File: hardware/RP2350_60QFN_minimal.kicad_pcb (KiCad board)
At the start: 4 copper layers, 106.9 x 43.5 mm, 138 parts, among them J1 UJ20-C-H-G-SMT-2A-P16-TR, J2 73101-0570, J3 73101-0570, J4 PinHeader_1x03, J5 4677, SW1 SW_Push, SW2 SW_Push, U1 RP2350_60QFN, U10 ADG621BRMZ, U13 TLP3441TP_F, U15 ADG621BRMZ, U2 REF35330QDBVR, U3 W25Q128JVS, U4 LM27762, U5 NCP1117-3.3_SOT223, U6 MCP47FEB02A0T-E/ST, U7 Opamp_Dual, U8 TLP3441TP_F, Y1 ABM8-272-T3

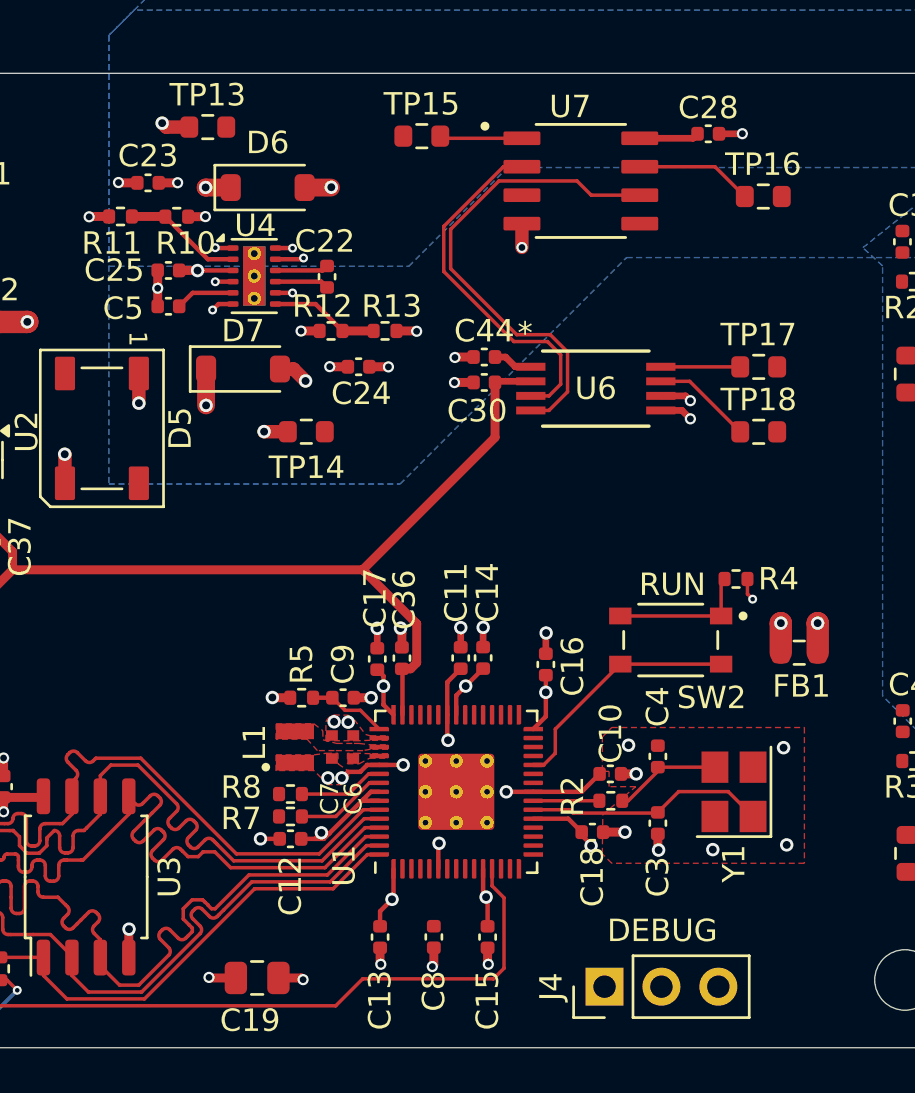
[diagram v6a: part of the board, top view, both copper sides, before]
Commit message: feat(hardware): Connect bottom layer data lines
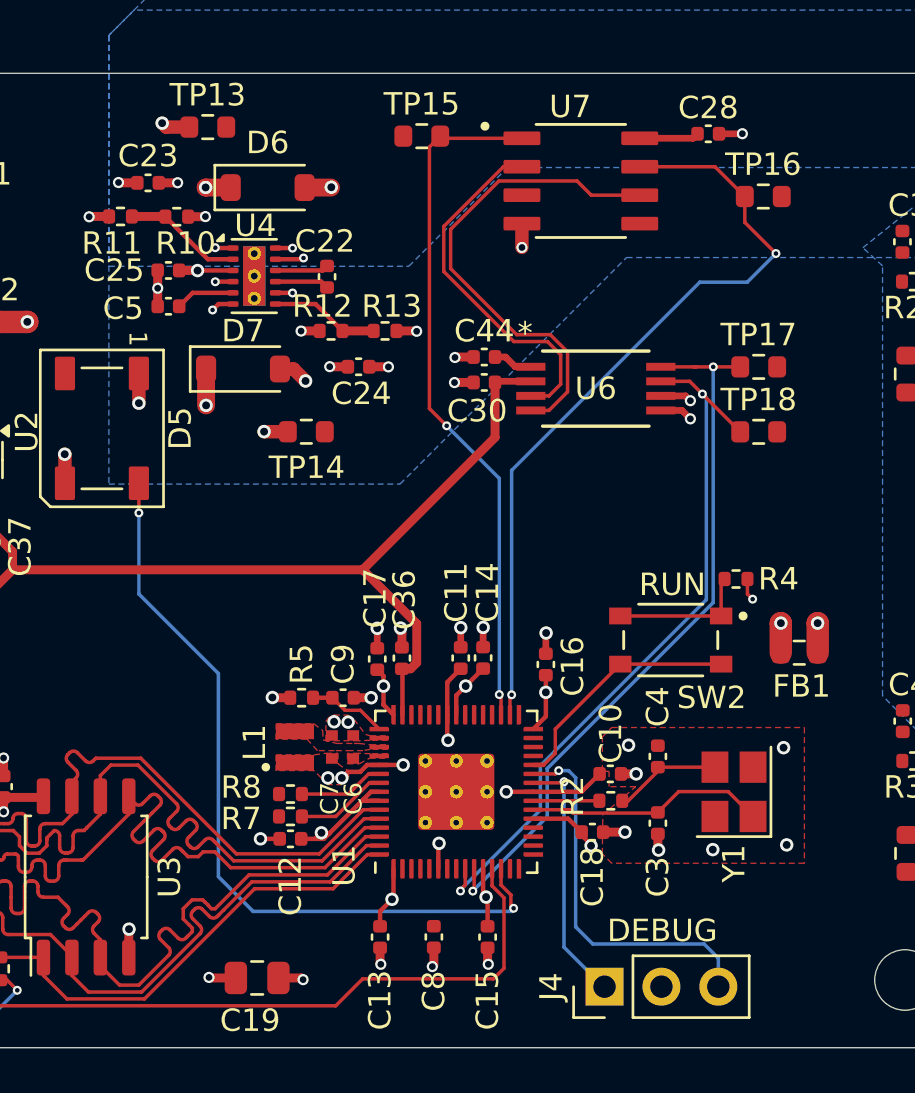
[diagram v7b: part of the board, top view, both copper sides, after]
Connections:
- U1 pad 32: /CHA_TRIG -> /CHB_TRIG
- U1 pad 33: /CHB_TRIG -> /CHA_TRIG
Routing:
- net /LED_DATA: track 0.00 -> 35.0 mm, vias 0 -> 2
- net /CHB_TRIG: track 5.24 -> 35.1 mm, vias 0 -> 2
- net /TRIG_SCL: track 3.55 -> 32.5 mm, vias 0 -> 2
- net /TRIG_SDA: track 4.48 -> 32.4 mm, vias 0 -> 2
- net /CHA_TRIG: track 3.68 -> 31.0 mm, vias 0 -> 2
- net /SWD: track 0.00 -> 17.0 mm, vias 0 -> 1
- net /SWCLK: track 0.00 -> 11.3 mm, vias 0 -> 1

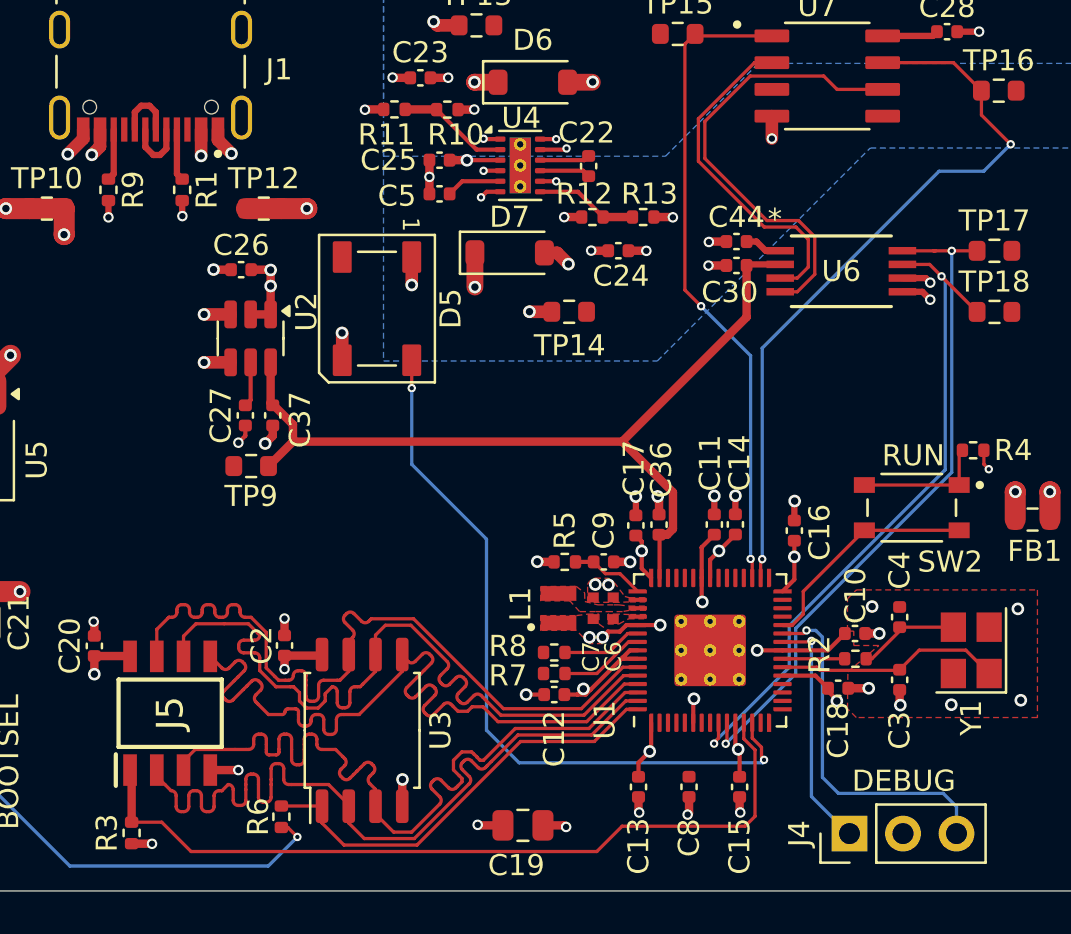
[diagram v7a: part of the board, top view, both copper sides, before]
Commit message: feat(hardware): Route USB data differential pair
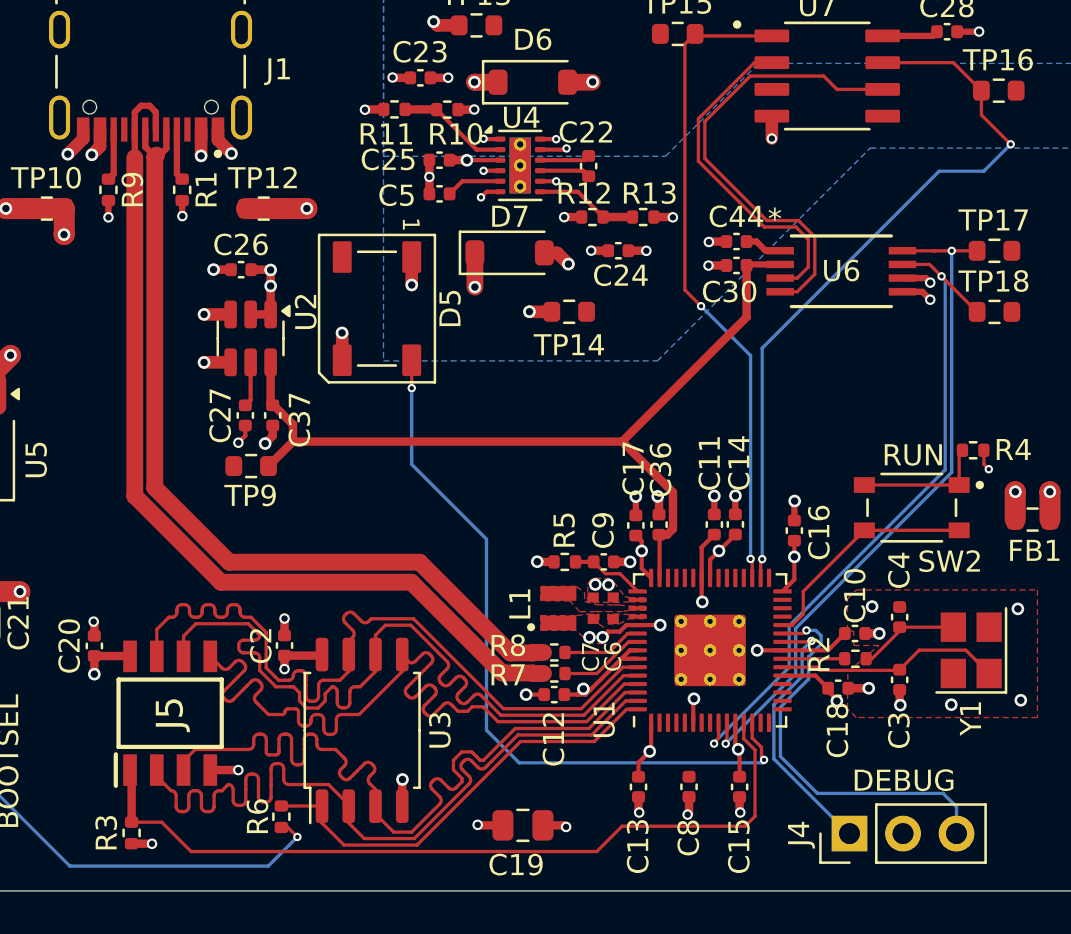
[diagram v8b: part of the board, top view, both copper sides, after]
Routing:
- net /USB_D+: track 2.91 -> 43.2 mm
- net /USB_D-: track 3.02 -> 40.6 mm
- net /SWD: track 17.0 -> 19.2 mm
- net /SWCLK: track 11.3 -> 12.8 mm
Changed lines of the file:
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@@
 	)
 	(segment
-		(start 141.3 126.67)
-		(end 141.3 133.33)
+		(start 140.984161 126.354161)
+		(end 141.24 126.61)
 		(width 0.156464)
 		(layer "B.Cu")
@@
 	)
 	(segment
-		(start 140.984161 126.354161)
-		(end 141.3 126.67)
+		(start 139.305129 132.330309)
+		(end 141.06482 134.09)
 		(width 0.156464)
 		(layer "B.Cu")
@@
 	)
 	(segment
+		(start 141.24 126.61)
+		(end 141.24 127.01)
+		(width 0.156464)
+		(layer "B.Cu")
+		(net 9)
+	)
+	(segment
+		(start 141.24 127.01)
+		(end 140.644928 127.605072)
+		(width 0.156464)
+		(layer "B.Cu")
+		(net 9)
+	)
+	(segment
 		(start 147.03 134.09)
 		(end 147.6674 134.7274)
@@
 	)
 	(segment
-		(start 142.06 134.09)
-		(end 147.03 134.09)
+		(start 139.305129 130.005022)
+		(end 139.305129 132.330309)
 		(width 0.156464)
 		(layer "B.Cu")
@@
 	)
 	(segment
+		(start 140.644928 127.605072)
+		(end 140.644928 128.665223)
+		(width 0.156464)
+		(layer "B.Cu")
+		(net 9)
+	)
+	(segment
+		(start 147.6674 134.7274)
+		(end 147.6674 136.000001)
+		(width 0.156464)
+		(layer "B.Cu")
+		(net 9)
+	)
+	(segment
 		(start 140.541998 126.354161)
 		(end 140.984161 126.354161)
@@
 	)
 	(segment
-		(start 147.6674 134.7274)
-		(end 147.6674 136.000001)
+		(start 140.644928 128.665223)
+		(end 139.305129 130.005022)
 		(width 0.156464)
 		(layer "B.Cu")
@@
 	)
 	(segment
-		(start 141.3 133.33)
-		(end 142.06 134.09)
+		(start 141.06482 134.09)
+		(end 147.03 134.09)
 		(width 0.156464)
 		(layer "B.Cu")
@@
 	)
 	(segment
-		(start 140.78 134.24)
-		(end 142.540001 136.000001)
+		(start 140.337464 127.292537)
+		(end 140.337464 128.537867)
 		(width 0.156464)
 		(layer "B.Cu")
@@
 	)
 	(segment
+		(start 140.337464 128.537867)
+		(end 138.997665 129.877666)
+		(width 0.156464)
+		(layer "B.Cu")
+		(net 10)
+	)
+	(segment
 		(start 142.540001 136.000001)
 		(end 142.5874 136.000001)
@@
 	)
 	(segment
+		(start 138.997665 132.457665)
+		(end 142.540001 136.000001)
+		(width 0.156464)
+		(layer "B.Cu")
+		(net 10)
+	)
+	(segment
+		(start 138.997665 129.877666)
+		(end 138.997665 132.457665)
+		(width 0.156464)
+		(layer "B.Cu")
+		(net 10)
+	)
+	(segment
 		(start 140.78 126.850001)
-		(end 140.78 134.24)
+		(end 140.337464 127.292537)
 		(width 0.156464)
 		(layer "B.Cu")
@@
 	)
 	(segment
+		(start 127.552399 128.375001)
+		(end 127.577399 128.400001)
+		(width 0.8)
+		(layer "F.Cu")
+		(net 16)
+	)
+	(segment
+		(start 121.783248 124.065)
+		(end 126.093249 128.375001)
+		(width 0.8)
+		(layer "F.Cu")
+		(net 16)
+	)
+	(segment
 		(start 109.346999 101.44)
 		(end 109.65 101.743001)
@@
 	)
 	(segment
+		(start 108.65 119.971752)
+		(end 112.743248 124.065)
+		(width 0.8)
+		(layer "F.Cu")
+		(net 16)
+	)
+	(segment
 		(start 108.953001 101.44)
 		(end 109.346999 101.44)
@@
 	)
 	(segment
+		(start 112.743248 124.065)
+		(end 121.783248 124.065)
+		(width 0.8)
+		(layer "F.Cu")
+		(net 16)
+	)
+	(segment
 		(start 109.65 101.743001)
 		(end 109.65 102.570001)
@@
 	)
 	(segment
+		(start 108.65 103.91)
+		(end 108.65 102.570001)
+		(width 0.3)
+		(layer "F.Cu")
+		(net 16)
+	)
+	(segment
+		(start 126.093249 128.375001)
+		(end 127.552399 128.375001)
+		(width 0.8)
+		(layer "F.Cu")
+		(net 16)
+	)
+	(segment
 		(start 108.65 101.743001)
 		(end 108.953001 101.44)
@@
 	)
 	(segment
+		(start 127.577399 128.400001)
+		(end 128.0574 128.400001)
+		(width 0.8)
+		(layer "F.Cu")
+		(net 16)
+	)
+	(segment
 		(start 108.65 102.570001)
 		(end 108.65 101.743001)
@@
 	)
 	(segment
+		(start 108.65 103.91)
+		(end 108.65 119.971752)
+		(width 0.8)
+		(layer "F.Cu")
+		(net 16)
+	)
+	(segment
+		(start 122.176752 123.115)
+		(end 126.486753 127.425001)
+		(width 0.8)
+		(layer "F.Cu")
+		(net 17)
+	)
+	(segment
+		(start 109.69 103.78)
+		(end 109.532999 103.78)
+		(width 0.3)
+		(layer "F.Cu")
+		(net 17)
+	)
+	(segment
 		(start 109.85 103.78)
-		(end 109.532999 103.78)
+		(end 109.69 103.78)
 		(width 0.3)
 		(layer "F.Cu")
@@
 	)
 	(segment
+		(start 109.601 119.579248)
+		(end 113.136752 123.115)
+		(width 0.8)
+		(layer "F.Cu")
+		(net 17)
+	)
+	(segment
+		(start 127.552399 127.425001)
+		(end 127.577399 127.400001)
+		(width 0.8)
+		(layer "F.Cu")
+		(net 17)
+	)
+	(segment
 		(start 109.532999 103.78)
 		(end 109.15 103.397001)
@@
 	)
 	(segment
+		(start 126.486753 127.425001)
+		(end 127.552399 127.425001)
+		(width 0.8)
+		(layer "F.Cu")
+		(net 17)
+	)
+	(segment
+		(start 113.136752 123.115)
+		(end 122.176752 123.115)
+		(width 0.8)
+		(layer "F.Cu")
+		(net 17)
+	)
+	(segment
+		(start 109.69 103.78)
+		(end 109.601 103.869)
+		(width 0.8)
+		(layer "F.Cu")
+		(net 17)
+	)
+	(segment
+		(start 127.577399 127.400001)
+		(end 128.0574 127.400001)
+		(width 0.8)
+		(layer "F.Cu")
+		(net 17)
+	)
+	(segment
 		(start 110.15 102.570001)
 		(end 110.15 103.48)
@@
 		(layer "F.Cu")
 		(net 17)
+	)
+	(segment
+		(start 109.601 103.869)
+		(end 109.601 119.579248)
+		(width 0.8)
+		(layer "F.Cu")
+		(net 17)
